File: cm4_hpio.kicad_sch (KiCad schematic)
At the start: 2 parts

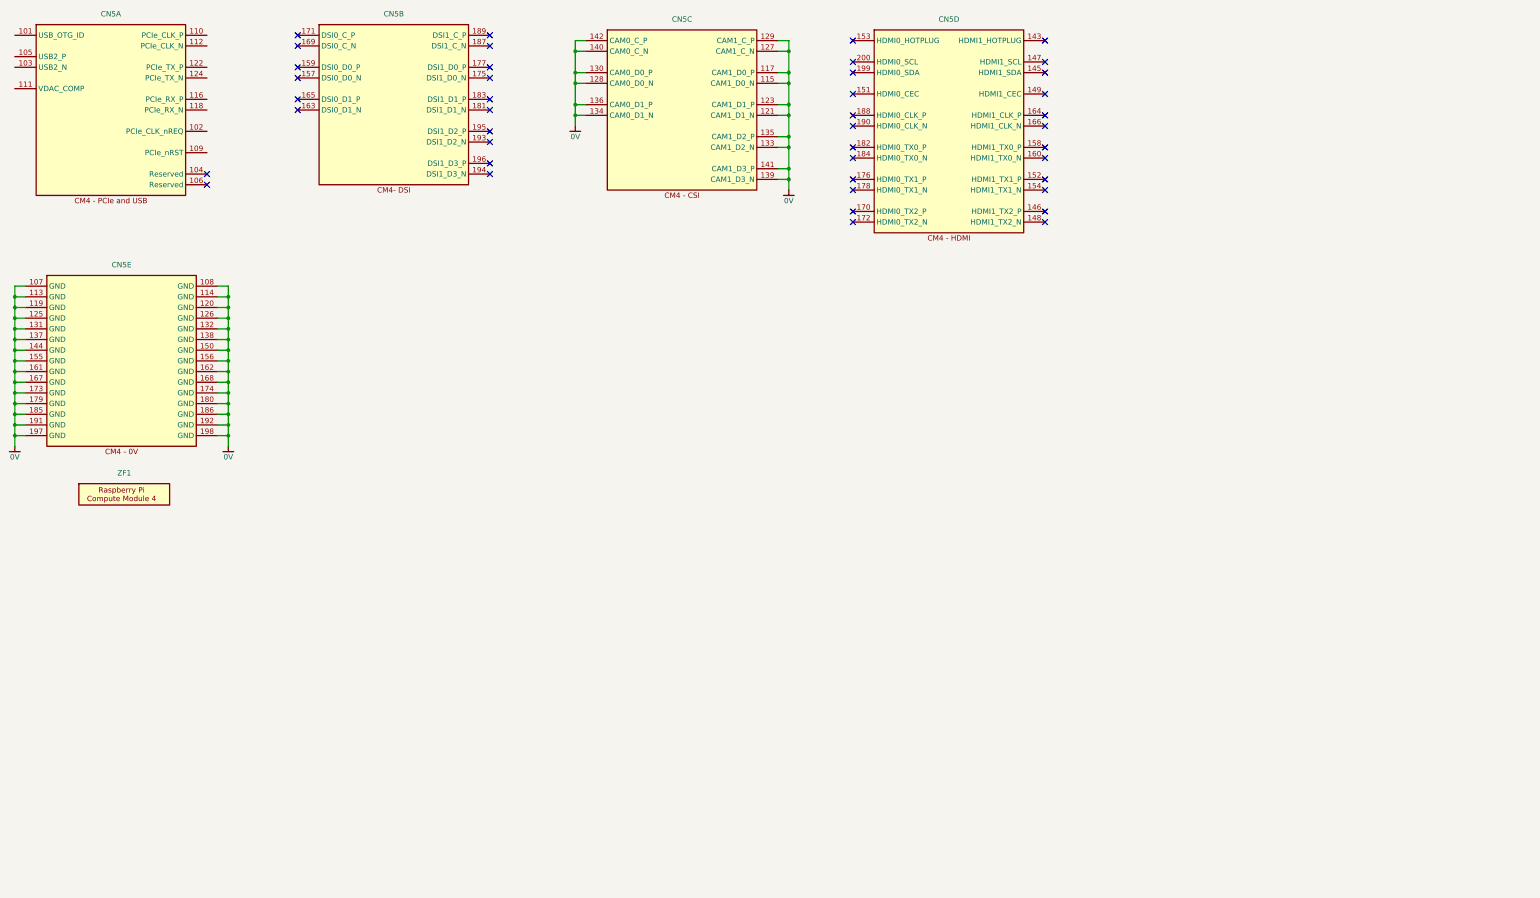
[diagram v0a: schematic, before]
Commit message: Added M.2 SSD
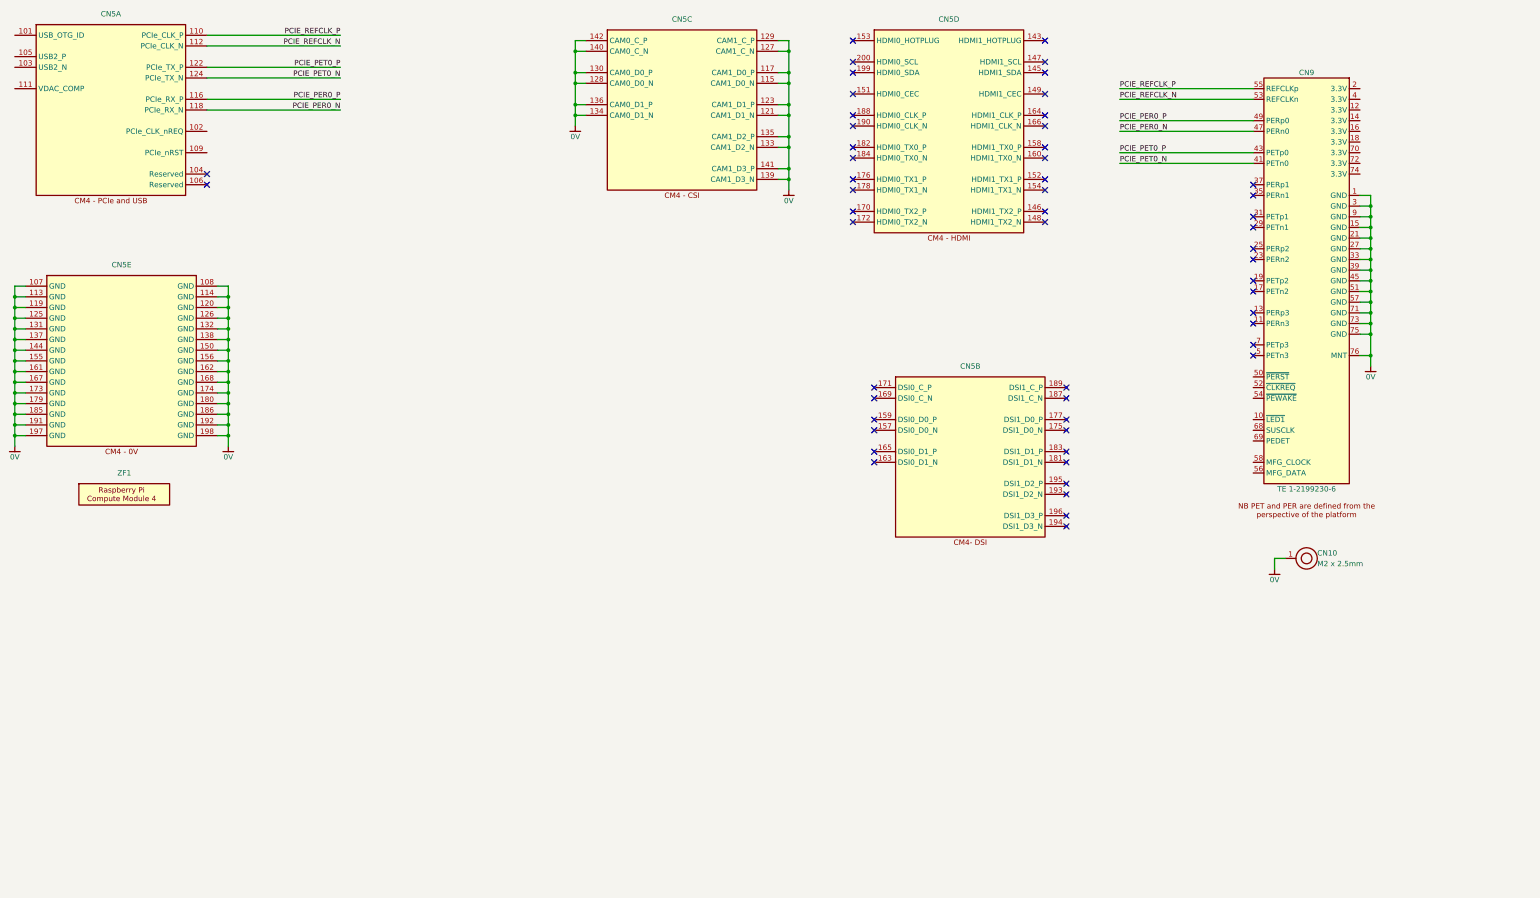
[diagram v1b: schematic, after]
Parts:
- added CN10: M2 x 2.5mm, Connector_WUT:Standoff_Wurth_9774025243R, symbol Connector_WUT:Wurth_9774025243R
- added CN9: TE 1-2199230-6, Connector_WUT:TE_1-2199230-6, symbol Connector_WUT:TE-Connectivity_M-2_1-2199230-6
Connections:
- net 0V: now also CN10.1, CN9.1 (GND), CN9.15 (GND), CN9.21 (GND), CN9.27 (GND), CN9.3 (GND), CN9.33 (GND), CN9.39 (GND), CN9.45 (GND), CN9.51 (GND), CN9.57 (GND), CN9.71 (GND), CN9.73 (GND), CN9.75 (GND), CN9.76 (MNT), CN9.9 (GND)
- net PCIE_REFCLK_P: now reaches CN5.110 (PCIe_CLK_P)
- net PCIE_REFCLK_P: now also CN9.55 (REFCLKp)
- net PCIE_REFCLK_N: now reaches CN5.112 (PCIe_CLK_N)
- net PCIE_REFCLK_N: now also CN9.53 (REFCLKn)
- net PCIE_PER0_P: now reaches CN5.116 (PCIe_RX_P)
- net PCIE_PER0_P: now also CN9.49 (PERp0)
- net PCIE_PER0_N: now reaches CN5.118 (PCIe_RX_N)
- net PCIE_PER0_N: now also CN9.47 (PERn0)
- net PCIE_PET0_P: now reaches CN5.122 (PCIe_TX_P)
- net PCIE_PET0_P: now also CN9.43 (PETp0)
- net PCIE_PET0_N: now reaches CN5.124 (PCIe_TX_N)
- net PCIE_PET0_N: now also CN9.41 (PETn0)
- no-connect marks 42 -> 54
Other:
- moved on the sheet: CN5B

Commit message: Added ESD and tided up PSU
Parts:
- added C123, C124: 22u, Capacitor_SMD:C_1206_3216Metric, symbol Auto_Library_WUT:Kyocera AVX 12063D226KAT2A
- added LD2: Green, LED_SMD:LED_0603_1608Metric, symbol Auto_Library_WUT:Ekinglux_E6C0603VGAC1UDA
- added R57: 1k0, Resistor_SMD:R_0402_1005Metric, symbol Auto_Library_WUT:KOA Speer RK73H1ETTP1001F
- added R58, R59: 100R, Resistor_SMD:R_0402_1005Metric, symbol Auto_Library_WUT:KOA Speer RK73H1ETTP1000F
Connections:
- net 0V: now also C123.2, C124.2
- net PCIE_PER0_N: now also CN9.41 (PERn0); no longer CN9.47 (PERn0)
- net PCIE_PER0_P: now also CN9.43 (PERp0); no longer CN9.49 (PERp0)
- net PCIE_PET0_N: now also CN9.47 (PETn0); no longer CN9.41 (PETn0)
- net PCIE_PET0_P: now also CN9.49 (PETp0); no longer CN9.43 (PETp0)
- net ~{PCIE_CLK_REQ}: now reaches CN5.102 (PCIe_CLK_nREQ)
- net ~{PCIE_CLK_REQ}: now also R59.1
- net at CN5.109 (PCIe_nRST): now also R58.1
- net at CN9.10 (~{LED1}): now also R57.2
- net 3V3_PCIE: now reaches CN9.12 (3.3V)
- net 3V3_PCIE: now also CN9.14 (3.3V), CN9.16 (3.3V), CN9.18 (3.3V), CN9.2 (3.3V), CN9.4 (3.3V), CN9.70 (3.3V), CN9.72 (3.3V), CN9.74 (3.3V), C123.1, C124.1
- net ~{PCIE_RST}: now reaches CN9.50 (~{PERST})
- net ~{PCIE_RST}: now also R58.2
- net at CN9.52 (~{CLKREQ}): now also R59.2
- new net: LD2.1 (K), R57.1
- new net 3V3: LD2.2 (A)
- no-connect marks 54 -> 59
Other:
- note added: "SSD Activity"

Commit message: started on power
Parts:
- added C128: 100n, Capacitor_SMD:C_0402_1005Metric, symbol Auto_Library_WUT:Yageo CC0402KRX7R8BB104
- added CN14: USB4110-GF-A, Connector_WUT:USB-C_GCT_USB4110-GF-A, symbol Connector_WUT:GCT_USB4110-GF-A
- added D8: USBLC6-2M6, Diode_WUT:TVS_ST_USBLC6-2M6, symbol Diode_WUT:USBLC6-2M6
- added FB25: 1k8, Inductor_SMD:L_0402_1005Metric, symbol Auto_Library_WUT:Murata BLM15BD182SN1D
- added FL1: 90R, Inductor_WUT:L_CommonMode_Wurth_WE-CNSW_0805, symbol Auto_Library_WUT:Wurth Elektronik 744231091
- added R61, R62: 5k1, Resistor_SMD:R_0402_1005Metric, symbol Auto_Library_WUT:KOA Speer RK73H1ETTP5101F
- added R63: 0R0, Resistor_SMD:R_0402_1005Metric, symbol Auto_Library_WUT:KOA Speer RK73Z1ETTP
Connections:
- net 0V: now also CN14.SH (SHIELD), FB25.1, R61.2, R62.2, R63.1
- net at CN5.101 (USB_OTG_ID): now also R63.2
- net at CN5.103 (USB2_N): now also FL1.4
- net at CN5.105 (USB2_P): now also FL1.2
- new net: CN14.A6 (DP1), CN14.B6 (DP2), D8.1, D8.6, FL1.1
- new net: C128.2, CN14.A1 (GND), CN14.A12 (GND), CN14.B1 (GND), CN14.B12 (GND), D8.2, FB25.2
- new net: CN14.A7 (DN1), CN14.B7 (DN2), D8.3, D8.4, FL1.3
- new net: C128.1, CN14.A4 (VBUS), CN14.A9 (VBUS), CN14.B4 (VBUS), CN14.B9 (VBUS), D8.5
- new net: CN14.A5 (CC1), R62.1
- new net: CN14.B5 (CC2), R61.1
- no-connect marks 59 -> 62
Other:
- moved on the sheet: CN5A, CN5E, R58, ZF1

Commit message: Schematic mostly done
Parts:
- added D18, D19: 3V3, Diode_SMD:D_SOD-523, symbol Auto_Library_WUT:nexperia PESD3V3U1UB,115
- added D3, D4: TPD4E05U06DQA, Diode_WUT:TPD4E05U06DQA, symbol Diode_WUT:TI_TPD4E05U06
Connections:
- net 0V: now also D18.2 (A), D19.2 (A), D3.3, D3.8, D4.3, D4.8
- net PCIE_PER0_N: now also D3.2, D3.9 (NC)
- net PCIE_PER0_P: now also D3.1, D3.10 (NC)
- net PCIE_PET0_N: now also D3.5, D3.6 (NC)
- net PCIE_PET0_P: now also D3.4, D3.7 (NC)
- net PCIE_REFCLK_N: now also D4.5, D4.6 (NC)
- net PCIE_REFCLK_P: now also D4.4, D4.7 (NC)
- net ~{PCIE_RST}: now also D19.1 (K)
- net at CN9.52 (~{CLKREQ}), R59.2: now also D18.1 (K)
- no-connect marks 62 -> 66
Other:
- moved on the sheet: CN5B, CN5D, R59

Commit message: schematic complete
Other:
- moved on the sheet: CN5B, CN5D
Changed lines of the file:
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@@
   (junction (at 294.64 191.77) (diameter 0) (color 0 0 0 0)
   )
+  (junction (at 52.07 200.66) (diameter 0) (color 0 0 0 0)
+  )
   (junction (at 243.84 201.93) (diameter 0) (color 0 0 0 0)
   )
@@
   (junction (at 347.98 58.42) (diameter 0) (color 0 0 0 0)
   )
-  (no_connect (at 140.335 40.005))
+  (no_connect (at 140.97 39.37))
   (no_connect (at 148.59 184.15))
   (no_connect (at 320.04 132.08))
-  (no_connect (at 160.655 102.87))
+  (no_connect (at 161.29 102.87))
   (no_connect (at 320.04 114.3))
   (no_connect (at 320.04 101.6))
   (no_connect (at 320.04 73.66))
-  (no_connect (at 206.375 102.87))
+  (no_connect (at 207.01 102.87))
   (no_connect (at 320.04 129.54))
-  (no_connect (at 160.655 100.33))
-  (no_connect (at 140.335 45.085))
-  (no_connect (at 160.655 80.01))
-  (no_connect (at 160.655 118.11))
-  (no_connect (at 160.655 115.57))
-  (no_connect (at 206.375 95.25))
+  (no_connect (at 161.29 100.33))
+  (no_connect (at 140.97 44.45))
+  (no_connect (at 161.29 80.01))
+  (no_connect (at 161.29 118.11))
+  (no_connect (at 161.29 115.57))
+  (no_connect (at 207.01 95.25))
   (no_connect (at 320.04 121.92))
-  (no_connect (at 206.375 92.71))
-  (no_connect (at 140.335 47.625))
+  (no_connect (at 207.01 92.71))
+  (no_connect (at 140.97 46.99))
   (no_connect (at 320.04 86.36))
-  (no_connect (at 94.615 32.385))
+  (no_connect (at 95.25 31.75))
   (no_connect (at 320.04 63.5))
-  (no_connect (at 94.615 45.085))
-  (no_connect (at 160.655 87.63))
+  (no_connect (at 95.25 44.45))
+  (no_connect (at 161.29 87.63))
   (no_connect (at 320.04 96.52))
-  (no_connect (at 94.615 29.845))
-  (no_connect (at 140.335 29.845))
-  (no_connect (at 160.655 110.49))
+  (no_connect (at 95.25 29.21))
+  (no_connect (at 140.97 29.21))
+  (no_connect (at 161.29 110.49))
   (no_connect (at 148.59 186.69))
   (no_connect (at 320.04 66.04))
   (no_connect (at 251.46 68.58))
-  (no_connect (at 140.335 32.385))
-  (no_connect (at 94.615 40.005))
-  (no_connect (at 206.375 118.11))
+  (no_connect (at 140.97 31.75))
+  (no_connect (at 95.25 39.37))
+  (no_connect (at 207.01 118.11))
   (no_connect (at 320.04 93.98))
-  (no_connect (at 94.615 37.465))
+  (no_connect (at 95.25 36.83))
   (no_connect (at 320.04 71.12))
-  (no_connect (at 206.375 74.93))
-  (no_connect (at 160.655 95.25))
-  (no_connect (at 140.335 62.865))
+  (no_connect (at 207.01 74.93))
+  (no_connect (at 161.29 95.25))
+  (no_connect (at 140.97 62.23))
   (no_connect (at 256.54 68.58))
-  (no_connect (at 160.655 92.71))
+  (no_connect (at 161.29 92.71))
   (no_connect (at 45.72 172.72))
   (no_connect (at 320.04 124.46))
-  (no_connect (at 160.655 107.95))
-  (no_connect (at 140.335 52.705))
-  (no_connect (at 140.335 60.325))
+  (no_connect (at 161.29 107.95))
+  (no_connect (at 140.97 52.07))
+  (no_connect (at 140.97 59.69))
   (no_connect (at 45.72 175.26))
   (no_connect (at 320.04 104.14))
-  (no_connect (at 160.655 74.93))
+  (no_connect (at 161.29 74.93))
   (no_connect (at 259.08 68.58))
-  (no_connect (at 94.615 47.625))
-  (no_connect (at 206.375 100.33))
-  (no_connect (at 206.375 107.95))
-  (no_connect (at 140.335 55.245))
-  (no_connect (at 206.375 82.55))
-  (no_connect (at 206.375 87.63))
+  (no_connect (at 95.25 46.99))
+  (no_connect (at 207.01 100.33))
+  (no_connect (at 207.01 107.95))
+  (no_connect (at 140.97 54.61))
+  (no_connect (at 207.01 82.55))
+  (no_connect (at 207.01 87.63))
   (no_connect (at 320.04 88.9))
   (no_connect (at 320.04 81.28))
   (no_connect (at 320.04 78.74))
-  (no_connect (at 206.375 115.57))
+  (no_connect (at 207.01 115.57))
   (no_connect (at 102.87 163.83))
-  (no_connect (at 206.375 80.01))
-  (no_connect (at 206.375 110.49))
+  (no_connect (at 207.01 80.01))
+  (no_connect (at 207.01 110.49))
   (no_connect (at 254 68.58))
-  (no_connect (at 140.335 37.465))
-  (no_connect (at 160.655 82.55))
+  (no_connect (at 140.97 36.83))
+  (no_connect (at 161.29 82.55))
   (wire (pts (xy 48.26 154.94) (xy 68.58 154.94))
     (stroke (width 0) (type default))
@@
     (stroke (width 0) (type default))
   )
-  (wire (pts (xy 48.26 200.66) (xy 55.88 200.66))
+  (wire (pts (xy 48.26 200.66) (xy 52.07 200.66))
     (stroke (width 0) (type default))
   )
@@
   )
   (wire (pts (xy 246.38 181.61) (xy 243.84 181.61))
+    (stroke (width 0) (type default))
+  )
+  (wire (pts (xy 52.07 200.66) (xy 55.88 200.66))
     (stroke (width 0) (type default))
   )
@@
     (property "Netclass" "USB" (at 97.409 157.48 0)
       (effects (font (size 1.27 1.27) italic) (justify left))
+    )
+  )
+  (symbol (lib_id "Power_WUT:PWR_FLAG") (at 52.07 200.66 0) (unit 1)
+    (in_bom yes) (on_board yes) (dnp no) (fields_autoplaced)
+    (property "Reference" "#FLG034" (at 52.07 198.755 0)
+      (effects (font (size 1.27 1.27)) hide)
+    )
+    (property "Value" "PWR_FLAG" (at 52.07 196.85 0)
+      (effects (font (size 1.27 1.27)) hide)
+    )
+    (property "Footprint" "" (at 52.07 200.66 0)
+      (effects (font (size 1.27 1.27)) hide)
+    )
+    (property "Datasheet" "~" (at 52.07 200.66 0)
+      (effects (font (size 1.27 1.27)) hide)
+    )
+    (pin "1")
+    (instances
+      (project "Master Timing Card"
+        (path "/6e8e281e-e30f-459d-852f-231836068db5/a795e361-f858-48e8-80c3-99d03ba37212"
+          (reference "#FLG034") (unit 1)
+        )
+      )
     )
   )
@@
     )
   )
-  (symbol (lib_id "Modules_WUT:ComputeModule4-HPIO") (at 183.515 74.93 0) (unit 4)
+  (symbol (lib_id "Modules_WUT:ComputeModule4-HPIO") (at 184.15 74.93 0) (unit 4)
     (in_bom yes) (on_board yes) (dnp no) (fields_autoplaced)
-    (property "Reference" "CN5" (at 183.515 69.85 0)
-      (effects (font (size 1.27 1.27)))
-    )
-    (property "Value" "~" (at 183.515 74.93 0)
-      (effects (font (size 1.27 1.27)))
-    )
-    (property "Footprint" "Connector_WUT:Hirose_DF40C-100DS-0.4V_pins-101-200" (at 183.515 74.93 0)
-      (effects (font (size 1.27 1.27)) hide)
-    )
-    (property "Datasheet" "" (at 183.515 74.93 0)
-      (effects (font (size 1.27 1.27)) hide)
-    )
-    (property "Manufacturer" "Hirose" (at 183.515 74.93 0)
-      (effects (font (size 1.27 1.27)) hide)
-    )
-    (property "MPN" "DF40C-100DS-0.4V(51)" (at 183.515 74.93 0)
+    (property "Reference" "CN5" (at 184.15 69.85 0)
+      (effects (font (size 1.27 1.27)))
+    )
+    (property "Value" "~" (at 184.15 74.93 0)
+      (effects (font (size 1.27 1.27)))
+    )
+    (property "Footprint" "Connector_WUT:Hirose_DF40C-100DS-0.4V_pins-101-200" (at 184.15 74.93 0)
+      (effects (font (size 1.27 1.27)) hide)
+    )
+    (property "Datasheet" "" (at 184.15 74.93 0)
+      (effects (font (size 1.27 1.27)) hide)
+    )
+    (property "Manufacturer" "Hirose" (at 184.15 74.93 0)
+      (effects (font (size 1.27 1.27)) hide)
+    )
+    (property "MPN" "DF40C-100DS-0.4V(51)" (at 184.15 74.93 0)
       (effects (font (size 1.27 1.27)) hide)
     )
@@
     )
   )
-  (symbol (lib_id "Modules_WUT:ComputeModule4-HPIO") (at 117.475 29.845 0) (unit 2)
+  (symbol (lib_id "Modules_WUT:ComputeModule4-HPIO") (at 118.11 29.21 0) (unit 2)
     (in_bom yes) (on_board yes) (dnp no) (fields_autoplaced)
-    (property "Reference" "CN5" (at 117.475 24.765 0)
-      (effects (font (size 1.27 1.27)))
-    )
-    (property "Value" "~" (at 117.475 29.845 0)
-      (effects (font (size 1.27 1.27)))
-    )
-    (property "Footprint" "Connector_WUT:Hirose_DF40C-100DS-0.4V_pins-101-200" (at 117.475 29.845 0)
-      (effects (font (size 1.27 1.27)) hide)
-    )
-    (property "Datasheet" "" (at 117.475 29.845 0)
-      (effects (font (size 1.27 1.27)) hide)
-    )
-    (property "Manufacturer" "Hirose" (at 117.475 29.845 0)
-      (effects (font (size 1.27 1.27)) hide)
-    )
-    (property "MPN" "DF40C-100DS-0.4V(51)" (at 117.475 29.845 0)
-      (effects (font (size 1.27 1.27)) hide)
-    )
+    (property "Reference" "CN5" (at 118.11 24.13 0)
+      (effects (font (size 1.27 1.27)))
+    )
+    (property "Value" "~" (at 118.11 29.21 0)
+      (effects (font (size 1.27 1.27)))
+    )
+    (property "Footprint" "Connector_WUT:Hirose_DF40C-100DS-0.4V_pins-101-200" (at 118.11 29.21 0)
+      (effects (font (size 1.27 1.27)) hide)
+    )
+    (property "Datasheet" "" (at 118.11 29.21 0)
+      (effects (font (size 1.27 1.27)) hide)
+    )
+    (property "Manufacturer" "Hirose" (at 118.11 29.21 0)
+      (effects (font (size 1.27 1.27)) hide)
+    )
+    (property "MPN" "DF40C-100DS-0.4V(51)" (at 118.11 29.21 0)
+      (effects (font (size 1.27 1.27)) hide)
+    )
